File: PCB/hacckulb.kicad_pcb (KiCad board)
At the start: 2 copper layers, 90.5 x 97.6 mm, 30 parts, among them SW1 SW_Push_45deg, SW10 SW_Push_45deg, SW11 SW_Push_45deg, SW14 RotaryEncoder_Switch, SW2 SW_Push_45deg, SW3 SW_Push_45deg, SW4 SW_Push_45deg, SW5 SW_Push_45deg, SW6 SW_Push_45deg, SW7 SW_Push_45deg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

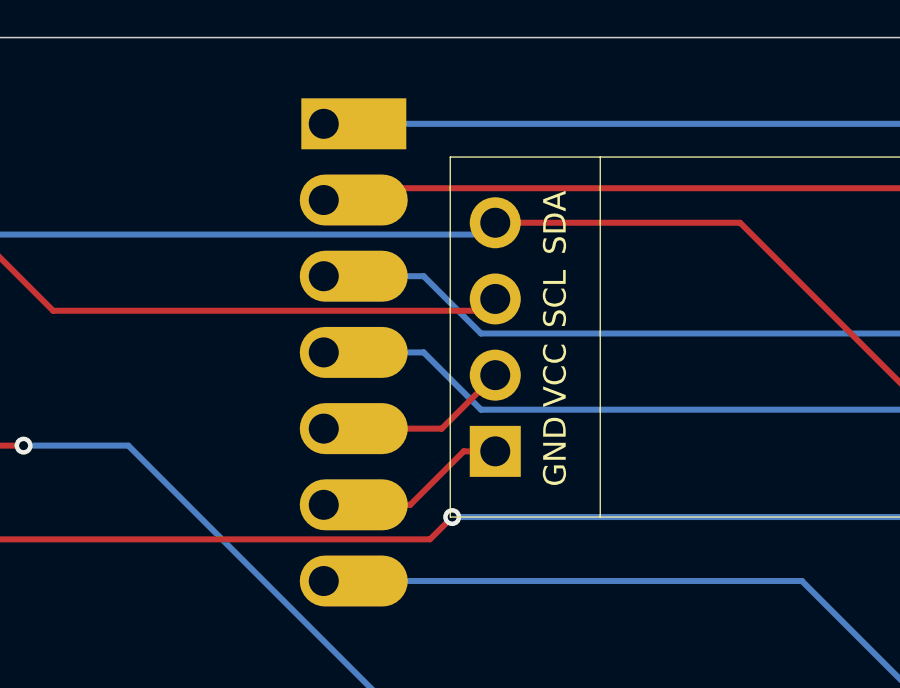
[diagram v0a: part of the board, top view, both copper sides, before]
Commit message: updated firmware and fixed pcb (which i printed wrong :( ))
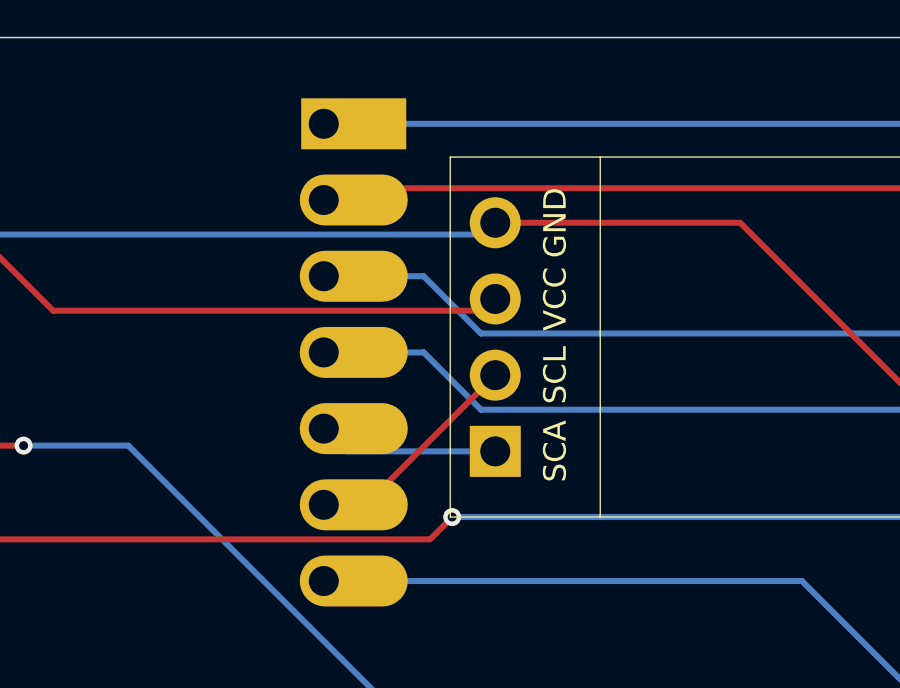
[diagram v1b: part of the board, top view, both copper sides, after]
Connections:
- U1 pad 5: SCL -> SDA
- U1 pad 6: SDA -> SCL
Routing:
- net SCL: track 6.45 -> 7.51 mm
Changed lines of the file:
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@@
 			(layer "F.CrtYd")
 		)
-		(fp_text user "SDA"
+		(fp_text user "GND"
 			(at 34.5 9.81 90)
 			(layer "F.SilkS")
@@
 			)
 		)
-		(fp_text user "SCL"
+		(fp_text user "VCC"
 			(at 34.5 7.27 90)
 			(layer "F.SilkS")
@@
 			)
 		)
-		(fp_text user "GND"
+		(fp_text user "SCA"
 			(at 34.5 2.19 90)
 			(layer "F.SilkS")
@@
 			)
 		)
-		(fp_text user "VCC"
+		(fp_text user "SCL"
 			(at 34.5 4.73 90)
 			(layer "F.SilkS")
@@
 			(layers "*.Cu" "*.Mask")
 			(remove_unused_layers no)
-			(net 18 "SCL")
+			(net 20 "SDA")
 			(pinfunction "PA8_A4_D4_SDA")
 			(pintype "passive")
@@
 			(layers "*.Cu" "*.Mask")
 			(remove_unused_layers no)
-			(net 20 "SDA")
+			(net 18 "SCL")
 			(pinfunction "PA9_A5_D5_SCL")
 			(pintype "passive")
@@
 	)
 	(segment
-		(start 173.48375 39.229156)
-		(end 169.55 39.229156)
+		(start 170.94375 41.769156)
+		(end 169.55 41.769156)
 		(width 0.2)
 		(layer "F.Cu")
@@
 	(segment
 		(start 175.26625 37.446656)
-		(end 173.48375 39.229156)
+		(end 170.94375 41.769156)
 		(width 0.2)
 		(layer "F.Cu")
@@
 	)
 	(segment
-		(start 174.21625 39.986656)
-		(end 172.43375 41.769156)
+		(start 170.3075 39.986656)
+		(end 169.55 39.229156)
 		(width 0.2)
-		(layer "F.Cu")
+		(layer "B.Cu")
 		(net 20)
 	)
 	(segment
 		(start 175.26625 39.986656)
-		(end 174.21625 39.986656)
+		(end 170.3075 39.986656)
 		(width 0.2)
-		(layer "F.Cu")
-		(net 20)
-	)
-	(segment
-		(start 172.43375 41.769156)
-		(end 169.55 41.769156)
-		(width 0.2)
-		(layer "F.Cu")
+		(layer "B.Cu")
 		(net 20)
 	)
